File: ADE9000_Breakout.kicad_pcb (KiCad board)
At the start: 2 copper layers, 65 x 55 mm, 61 parts, among them J1 DIGITAL, J2 Voltage, J3 Voltage, J4 Voltage, U1 ADE9000, Y1 24.576MHz

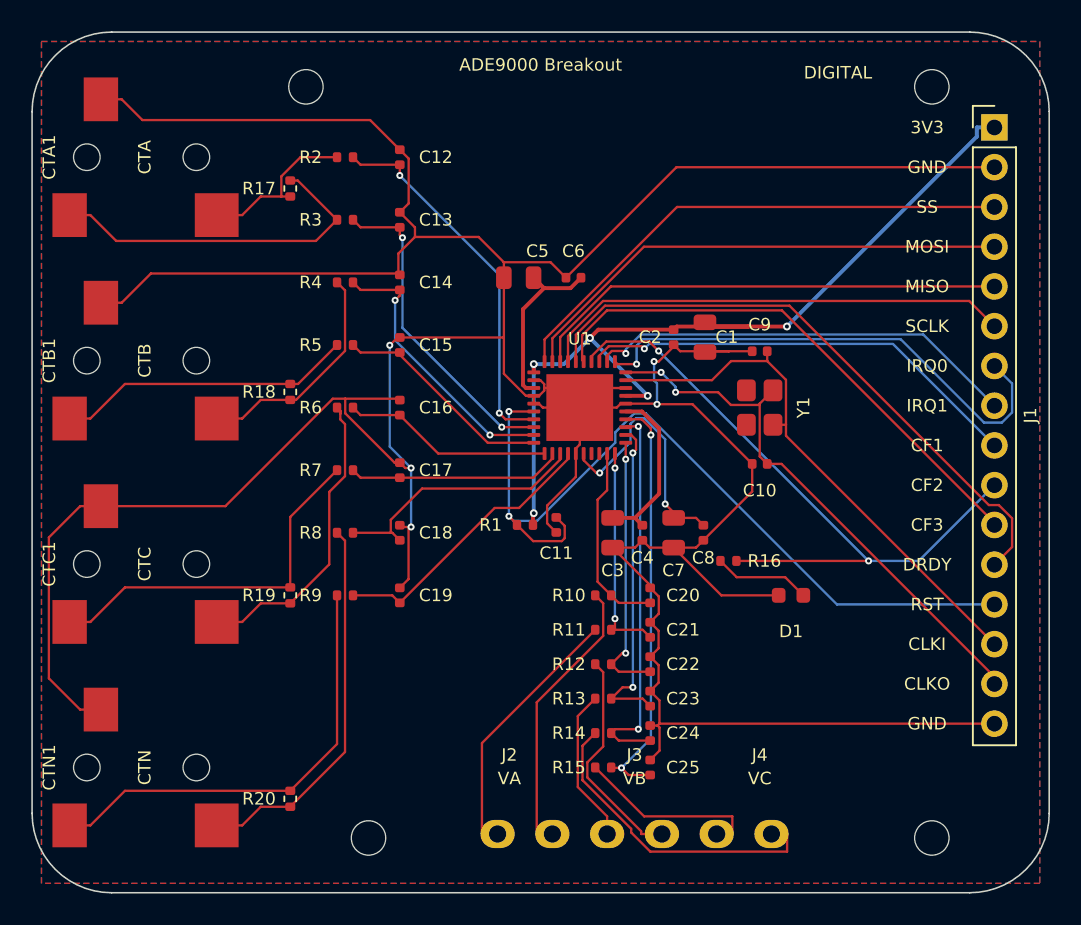
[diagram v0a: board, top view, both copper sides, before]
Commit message: Use SparkFun locking digital header
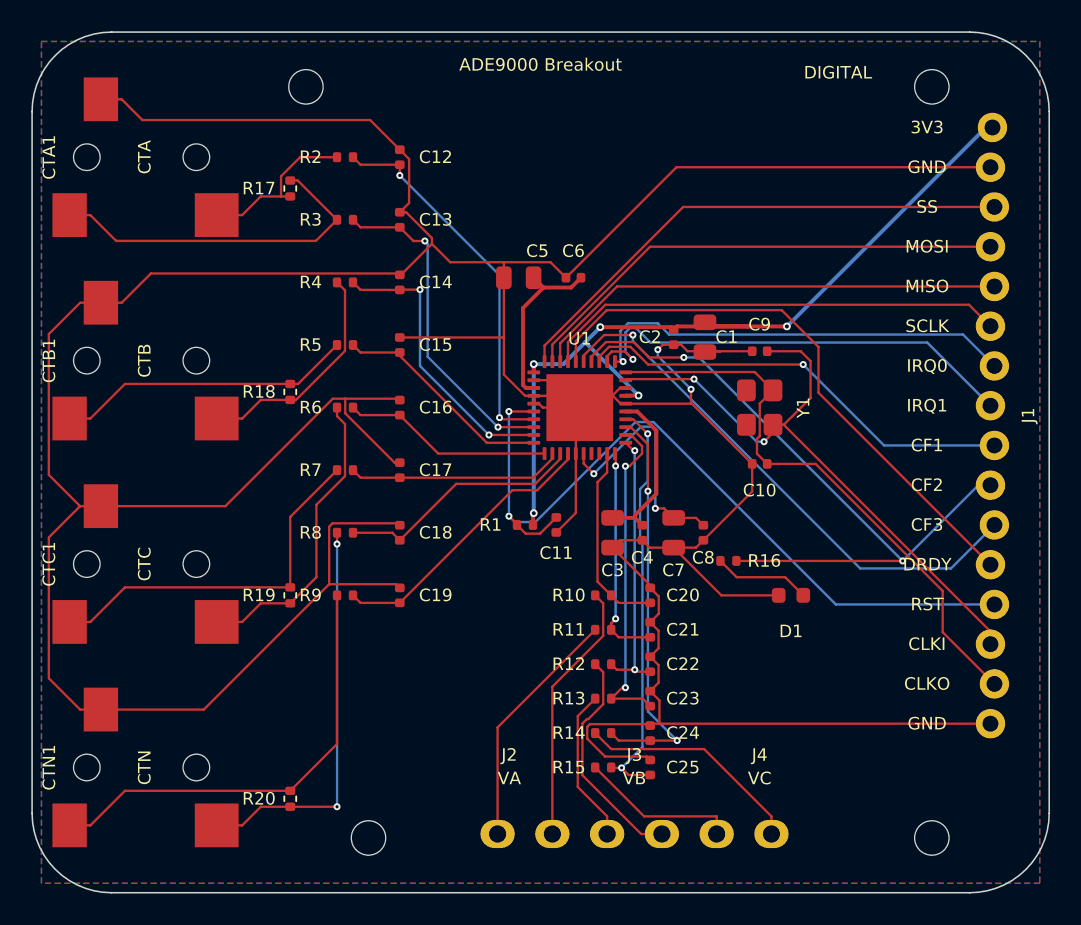
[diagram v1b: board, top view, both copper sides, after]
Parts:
- J1: footprint PinHeader_1x16_P2.54mm_Vertical -> 1x16_Locking
- moved J1 0.13 mm to (184.9, 86.1), turned to -90 degrees
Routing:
- net GND: track 273.5 -> 308.6 mm, vias 5 -> 2
- net VCN_J: track 19.6 -> 14.6 mm
- net IRQ0: track 32.7 -> 27.8 mm
- net CLKIN: track 35.1 -> 39.8 mm, vias 0 -> 2
- net RESET: track 53.6 -> 50.9 mm
- net CF4_DREADY: track 39.4 -> 37.1 mm
- net CF2: track 42.7 -> 44.6 mm
- net IRQ1: track 27.9 -> 29.7 mm
- net CLKOUT: track 35.5 -> 37.2 mm, vias 2 -> 0
- net +3V3: track 56.4 -> 55.0 mm
- net INP_J: track 24.4 -> 25.7 mm, vias 0 -> 2
- net VCN: track 24.8 -> 26.0 mm
- net VCP_J: track 11.2 -> 10.2 mm
- net INP: track 16.8 -> 15.9 mm
- net REF: track 16.0 -> 15.3 mm
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
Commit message: Add 12 VAC voltage input support
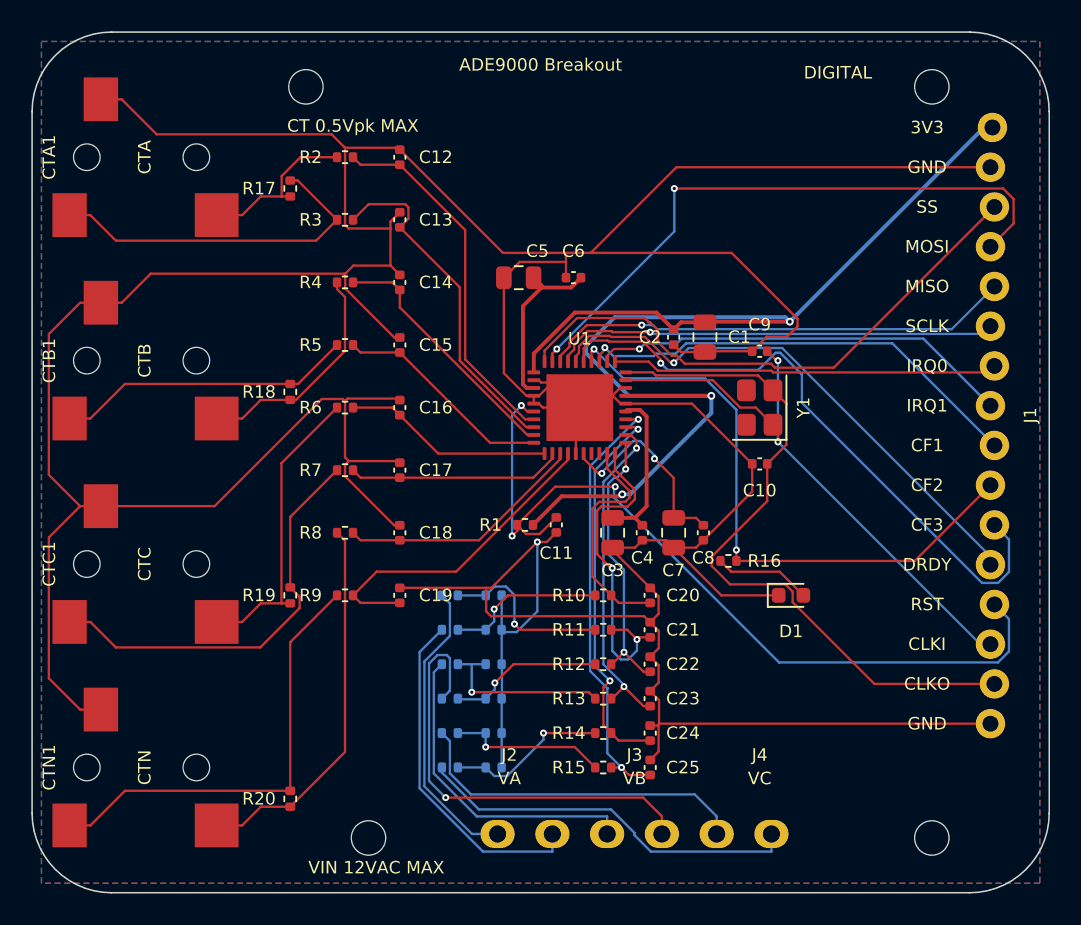
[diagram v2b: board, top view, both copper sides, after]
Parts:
- added R21: 100k, R_0402_1005Metric, B.Cu at (150.2, 116.0)
- added R22: 100k, R_0402_1005Metric, B.Cu at (150.2, 118.2)
- added R23: 100k, R_0402_1005Metric, B.Cu at (150.2, 120.4)
- added R24: 100k, R_0402_1005Metric, B.Cu at (150.2, 122.6)
- added R25: 100k, R_0402_1005Metric, B.Cu at (150.2, 124.8)
- added R26: 100k, R_0402_1005Metric, B.Cu at (150.2, 127.0)
- added R27: 2.49k, R_0402_1005Metric, B.Cu at (153.0, 116.0)
- added R28: 2.49k, R_0402_1005Metric, B.Cu at (153.0, 118.2)
- added R29: 2.49k, R_0402_1005Metric, B.Cu at (153.0, 120.4)
- added R30: 2.49k, R_0402_1005Metric, B.Cu at (153.0, 122.6)
- added R31: 2.49k, R_0402_1005Metric, B.Cu at (153.0, 124.8)
- added R32: 2.49k, R_0402_1005Metric, B.Cu at (153.0, 127.0)
- J2, J3, J4: footprint TerminalBlock_4Ucon:TerminalBlock_4Ucon_1x02_P3.50mm_Horizontal -> ADE9000-Local:TerminalBlock_4Ucon_1x02_P3.50mm_Horizontal_ADE9000
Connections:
- R10 pad 1: VAN_J -> VAN_DIV
- R11 pad 1: VAP_J -> VAP_DIV
- R12 pad 1: VBN_J -> VBN_DIV
- R13 pad 1: VBP_J -> VBP_DIV
- R14 pad 1: VCN_J -> VCN_DIV
- R15 pad 1: VCP_J -> VCP_DIV
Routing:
- net +3V3: track 55.0 -> 81.8 mm, vias 5 -> 3
- net GND: track 308.6 -> 332.0 mm, vias 2 -> 1
- net VBN_J: track 14.5 -> 28.9 mm, vias 0 -> 1
- net VCP_J: track 10.2 -> 22.1 mm
- net VBP_DIV: track 0.00 -> 11.6 mm, vias 0 -> 1
- net VAP_DIV: track 0.00 -> 11.2 mm, vias 0 -> 1
- net VBP_J: track 9.89 -> 20.5 mm
- net VCN_DIV: track 0.00 -> 10.4 mm, vias 0 -> 1
- net VCP_DIV: track 0.00 -> 10.2 mm, vias 0 -> 1
- net VAN_DIV: track 0.00 -> 10.1 mm, vias 0 -> 1
- net VCN_J: track 14.6 -> 24.7 mm
- net VBN_DIV: track 0.00 -> 9.97 mm, vias 0 -> 1
- net MOSI: track 31.7 -> 39.9 mm, vias 0 -> 2
- net CLKOUT: track 37.2 -> 45.0 mm
- net VAP: track 14.1 -> 21.1 mm
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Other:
- board text added: "CT 0.5Vpk MAX"
- board text added: "VIN 12VAC MAX"

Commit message: Move SMD parts to front side
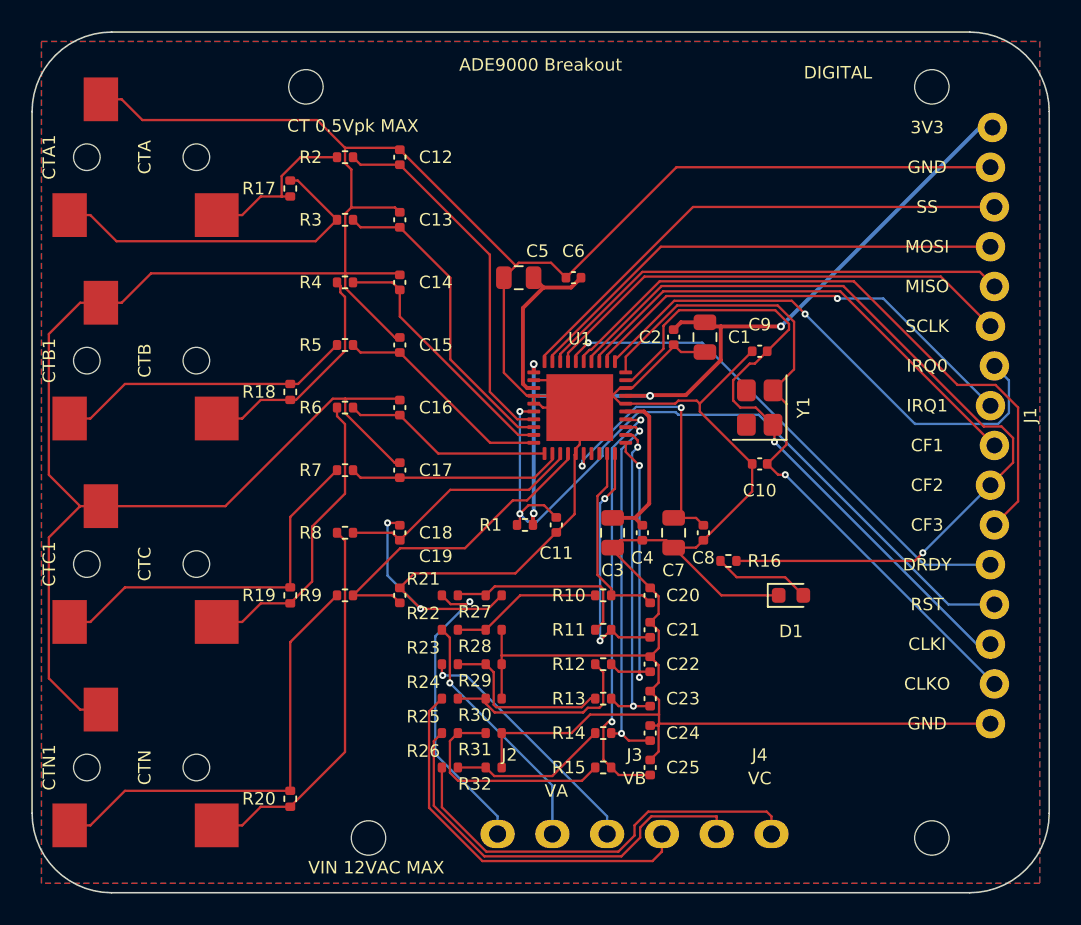
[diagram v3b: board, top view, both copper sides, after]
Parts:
- R21, R22, R23, R24, R25, R26, R27, R28, R29, R30, R31, R32: moved to F.Cu
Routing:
- net +3V3: track 81.8 -> 53.4 mm, vias 3 -> 4
- net CF2: track 39.5 -> 55.0 mm, vias 2 -> 1
- net IRQ0: track 24.7 -> 33.8 mm, vias 0 -> 1
- net MOSI: track 39.9 -> 31.3 mm, vias 2 -> 0
- net CLKIN: track 36.9 -> 43.5 mm, vias 2 -> 1
- net VAN_J: track 22.0 -> 16.0 mm, vias 0 -> 1
- net VAP: track 21.1 -> 16.1 mm
- net REF: track 13.1 -> 18.1 mm
- net RESET: track 54.7 -> 49.9 mm, vias 3 -> 2
- net VCP_J: track 22.1 -> 26.8 mm
- net VBP_J: track 20.5 -> 16.1 mm, vias 0 -> 1
- net VCP_DIV: track 10.2 -> 14.4 mm, vias 1 -> 0
- net VBN_J: track 28.9 -> 25.0 mm, vias 1 -> 0
- net GND: track 332.0 -> 328.1 mm, vias 1 -> 2
- net SS: track 36.3 -> 33.1 mm
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
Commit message: Use 0603 passives for hand assembly
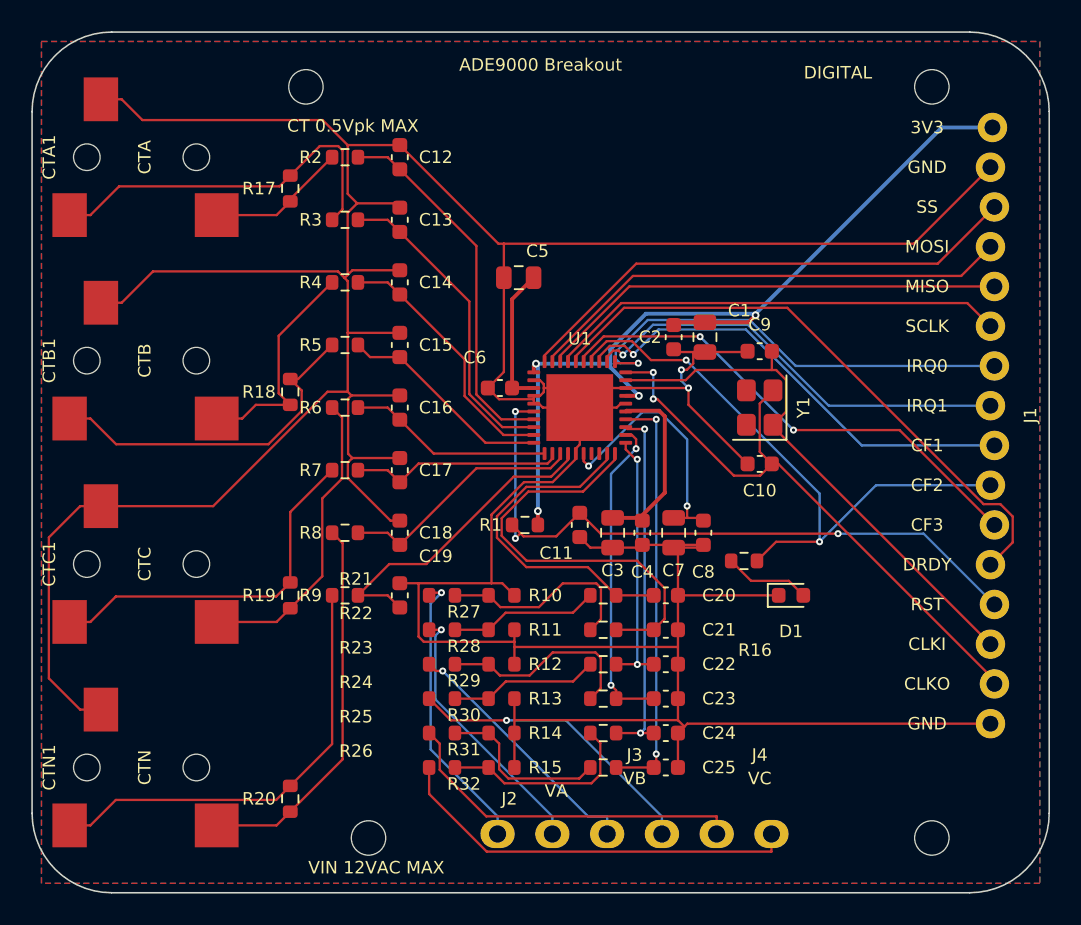
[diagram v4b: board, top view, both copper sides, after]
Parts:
- C10, C11, C12, C13, C14, C15, C16, C17, C18, C19, C2, C20, C21, C22, C23, C24, C25, C4, C6, C8, C9: footprint Capacitor_SMD:C_0402_1005Metric -> C_0603_1608Metric
- R1, R10, R11, R12, R13, R14, R15, R16, R2, R3, R4, R5, R6, R7, R8, R9: footprint Resistor_SMD:R_0402_1005Metric -> R_0603_1608Metric
- R17, R18, R19, R20, R21, R22, R23, R24, R25, R26, R27, R28, R29, R30, R31, R32: footprint R_0402_1005Metric -> R_0603_1608Metric
- moved C6 8.47 mm to (153.4, 102.8)
- moved C11 1.50 mm to (158.5, 111.5)
- moved C20 1.00 mm to (164.0, 116.0), turned to 0 degrees
- moved C21 1.00 mm to (164.0, 118.2), turned to 0 degrees
- moved C22 1.00 mm to (164.0, 120.4), turned to 0 degrees
- moved C23 1.00 mm to (164.0, 122.6), turned to 0 degrees
- moved C24 1.00 mm to (164.0, 124.8), turned to 0 degrees
- moved C25 1.00 mm to (164.0, 127.0), turned to 0 degrees
- moved R16 1.00 mm to (169.0, 113.8)
- moved R21 0.50 mm to (149.7, 116.0)
- moved R22 0.50 mm to (149.7, 118.2)
- moved R23 0.50 mm to (149.7, 120.4)
- moved R24 0.50 mm to (149.7, 122.6)
- moved R25 0.50 mm to (149.7, 124.8)
- moved R26 0.50 mm to (149.7, 127.0)
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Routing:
- net CF2: track 55.0 -> 39.4 mm, vias 1 -> 2
- net GND: track 328.1 -> 313.0 mm
- net VAP: track 16.1 -> 27.5 mm, vias 2 -> 0
- net CF3_ZX: track 41.6 -> 32.1 mm, vias 0 -> 2
- net VAN: track 12.4 -> 21.8 mm
- net CLKIN: track 43.5 -> 35.0 mm, vias 1 -> 0
- net RESET: track 49.9 -> 43.9 mm, vias 2 -> 3
- net VBN_J: track 25.0 -> 19.1 mm, vias 0 -> 1
- net CF4_DREADY: track 33.1 -> 38.7 mm, vias 1 -> 0
- net CLKOUT: track 44.4 -> 38.9 mm, vias 1 -> 2
- net VCP_J: track 26.8 -> 22.7 mm
- net IRQ0: track 33.8 -> 29.8 mm
- net VCP_DIV: track 14.4 -> 11.1 mm
- net IBN_J: track 19.0 -> 22.3 mm
- net VBN_DIV: track 12.8 -> 9.56 mm
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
